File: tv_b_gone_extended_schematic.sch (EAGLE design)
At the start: 24 parts, among them IC1 ATMEGA644PV-10PU, IC2 MCP1825S-3302E_DB, Q5 MPS2907A, T1 2N3904, T2 2N3904, T3 2N3904, T4 2N3904, U1 PEC11R-4015F-S0024

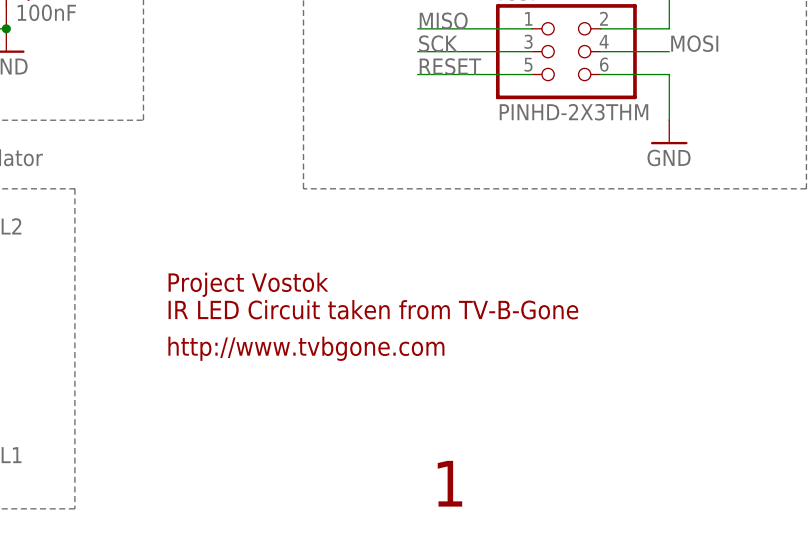
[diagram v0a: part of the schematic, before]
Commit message: remove garbage files and add detail to schem
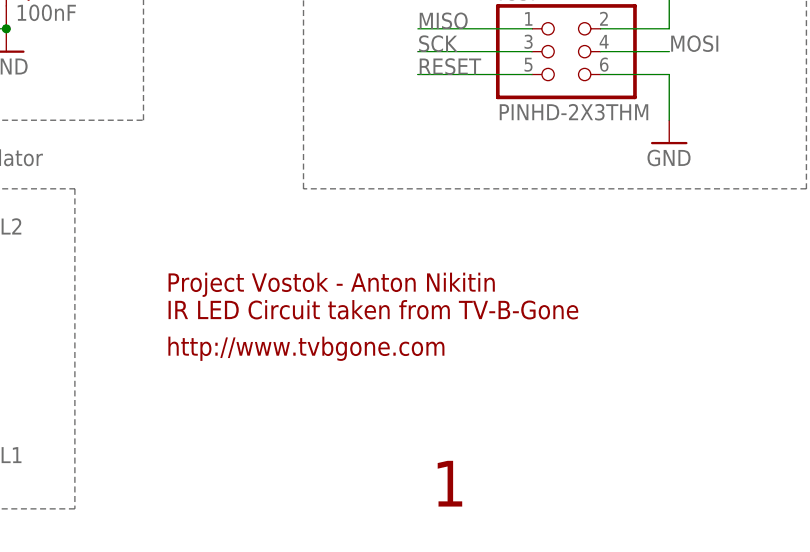
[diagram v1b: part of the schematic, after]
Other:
- note added: "Project Vostok - Anton Nikitin IR LED Circuit taken from TV-B-Gone"
- note removed: "Project Vostok IR LED Circuit taken from TV-B-Gone"
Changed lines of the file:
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@@
 <text x="134.62" y="73.66" size="1.778" layer="95">UNUSED</text>
 <text x="198.12" y="-41.402" size="2.032" layer="94">http://www.tvbgone.com</text>
-<text x="198.12" y="-37.338" size="2.032" layer="94">Project Vostok
+<text x="198.12" y="-37.338" size="2.032" layer="94">Project Vostok - Anton Nikitin
 IR LED Circuit taken from TV-B-Gone</text>
 <text x="287.02" y="-58.42" size="2.54" layer="94">v1.0</text>
